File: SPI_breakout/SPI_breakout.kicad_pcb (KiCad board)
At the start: 2 copper layers, 35 x 45 mm, 10 parts, among them J1 OPC-N3 A terminal, J2 OPC-N3 B terminal, J3 External OPC 5V input, U1 WisBlock IO Connector, U2 Adafruit 4682 microSD

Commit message: Reworking routing
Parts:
- added GAS1: Screw_Terminal_01x04, MyParts:CONN_1984633_PXC, F.Cu at (2.70, -40.8)
- J1: value OPC-N3 A terminal -> OPC-N3 A
- J2: value OPC-N3 B terminal -> OPC-N3 B
- J3: value External OPC 5V input -> External OPC 5V Input
- U1: value WisBlock IO Connector -> ~
- U2: value Adafruit 4682 microSD -> ~
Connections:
- J1 pad 1: /GND -> GND
- J2 pad 1: /GND -> GND
- J3 pad 2: /GND -> GND
- U1 pad 1: (no net) -> unconnected-(U1-NC-Pad1)
- U1 pad 10: (no net) -> unconnected-(U1-SW1-Pad10)
- U1 pad 11: (no net) -> unconnected-(U1-TXD0-Pad11)
- U1 pad 12: (no net) -> unconnected-(U1-RXD0-Pad12)
- U1 pad 13: (no net) -> unconnected-(U1-RST-Pad13)
- U1 pad 14: (no net) -> unconnected-(U1-LED1-Pad14)
- U1 pad 15: (no net) -> unconnected-(U1-LED2-Pad15)
- U1 pad 16: (no net) -> unconnected-(U1-NC-Pad16)
- U1 pad 17: (no net) -> Net-(GAS1-VCC)
- U1 pad 19: (no net) -> Net-(GAS1-SDA)
- U1 pad 2: (no net) -> unconnected-(U1-NC-Pad2)
- U1 pad 20: (no net) -> Net-(GAS1-SCL)
- U1 pad 21: (no net) -> unconnected-(U1-AIN0-Pad21)
- U1 pad 22: (no net) -> unconnected-(U1-AIN1-Pad22)
- U1 pad 23: (no net) -> unconnected-(U1-NC-Pad23)
- U1 pad 24: (no net) -> unconnected-(U1-IO7-Pad24)
- U1 pad 3: /GND -> unconnected-(U1-GND-Pad3)
- U1 pad 30: (no net) -> unconnected-(U1-NC-Pad30)
- U1 pad 32: (no net) -> unconnected-(U1-IO4-Pad32)
- U1 pad 33: (no net) -> unconnected-(U1-TXD1-Pad33)
- U1 pad 34: (no net) -> unconnected-(U1-RXD1-Pad34)
- U1 pad 35: (no net) -> Net-(GAS2-SDA)
- U1 pad 36: (no net) -> Net-(GAS2-SCL)
- U1 pad 37: (no net) -> unconnected-(U1-IO5-Pad37)
- U1 pad 38: (no net) -> unconnected-(U1-IO6-Pad38)
- U1 pad 39: /GND -> unconnected-(U1-GND-Pad39)
- U1 pad 4: /GND -> Net-(GAS2-GND)
- U1 pad 40: /GND -> GND
- U1 pad 5: (no net) -> Net-(GAS2-VCC)
- U1 pad 6: (no net) -> unconnected-(U1-3v3_S-Pad6)
- U1 pad 7: (no net) -> unconnected-(U1-NC-Pad7)
- U1 pad 8: (no net) -> unconnected-(U1-NC-Pad8)
- U1 pad 9: (no net) -> unconnected-(U1-NC-Pad9)
- U1 pad MP1: /GND -> (no net)
- U1 pad MP2: /GND -> (no net)
- U1 pad MP3: /GND -> (no net)
- U1 pad MP4: /GND -> (no net)
- U2 pad 2: /GND -> GND
- U2 pad 7: (no net) -> unconnected-(U2-DAT1-Pad7)
- U2 pad 8: (no net) -> unconnected-(U2-DAT2-Pad8)
- U2 pad 9: (no net) -> unconnected-(U2-DET-Pad9)
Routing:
- net Net-(GAS1-SCL): track 0.00 -> 28.1 mm, vias 0 -> 2
- net /SPI_MISO: track 65.2 -> 40.0 mm, vias 3 -> 2
- net /SPI_MOSI: track 56.6 -> 34.6 mm, vias 3 -> 2
- net Net-(GAS1-SDA): track 0.00 -> 21.3 mm
- net Net-(GAS1-VCC): track 0.00 -> 17.9 mm, vias 0 -> 1
- net /OPC1_CS: track 43.7 -> 34.6 mm, vias 0 -> 2
- net GND: track 0.00 -> 7.01 mm
- net /OPC2_CS: track 20.0 -> 20.7 mm
- added copper zone on B.Cu, net GND
- added copper zone on F.Cu, net GND
- removed copper zone on B.Cu, net /GND
- removed copper zone on F.Cu, net /GND
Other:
- board text added: "EFD"
- board text removed: "RAK holes"

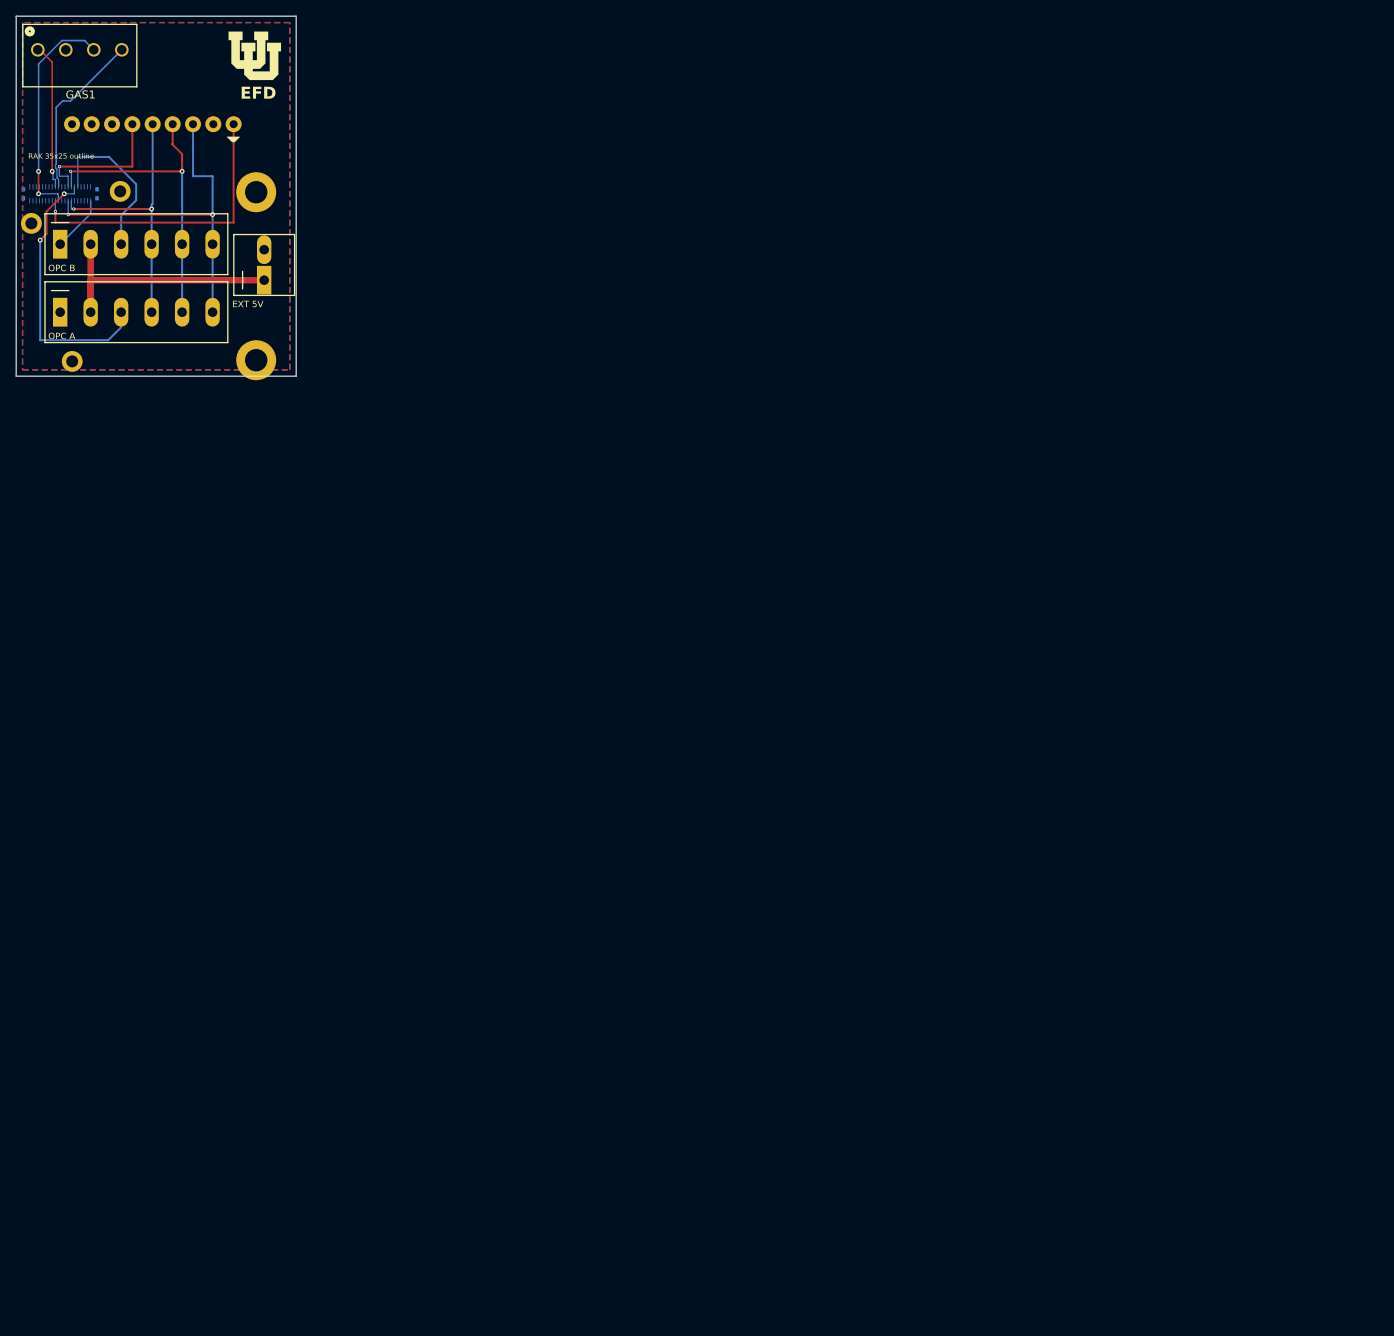
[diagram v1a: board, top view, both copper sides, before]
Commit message: Rework into smaller footprint and add 3D models
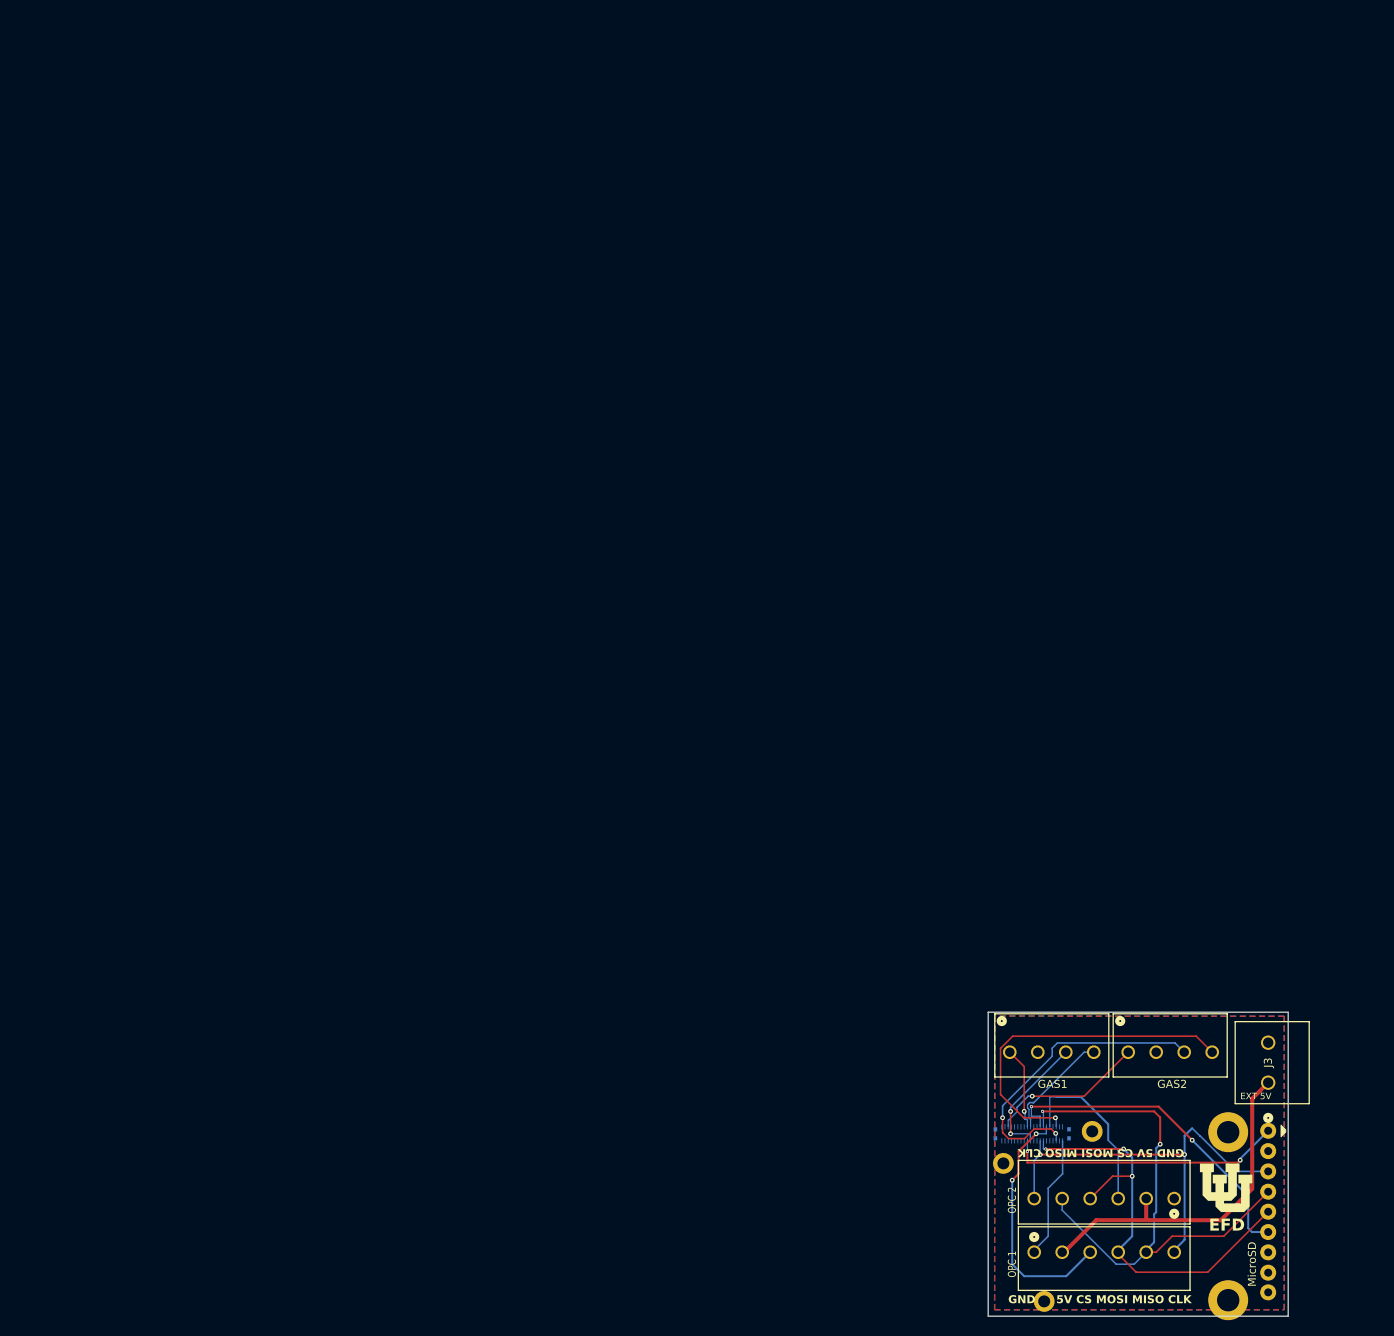
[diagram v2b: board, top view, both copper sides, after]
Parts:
- added GAS2: Screw_Terminal_01x04, MyParts:CONN_1984633_PXC, F.Cu at (139.0, 84.5)
- J1: value OPC-N3 A -> OPC 1; footprint Connector_Phoenix_MC:PhoenixContact_MC_1,5_6-G-3.81_1x06_P3.81mm_Horizontal -> MyParts:CONN_1984659_PXC
- J2: value OPC-N3 B -> OPC 2; footprint Connector_Phoenix_MC:PhoenixContact_MC_1,5_6-G-3.81_1x06_P3.81mm_Horizontal -> MyParts:CONN_1984659_PXC
- J3: footprint Connector_Phoenix_MC:PhoenixContact_MC_1,5_2-G-3.81_1x02_P3.81mm_Horizontal -> MyParts:CONN_1935161_PXC
- U2: value ~ -> MicroSD
- moved U2 194.8 mm to (156.5, 104.5), turned to -90 degrees
- moved J2 183.4 mm to (144.8, 102.8), turned to 180 degrees
- moved GAS1 174.5 mm to (124.2, 84.5)
- moved J1 169.2 mm to (127.2, 109.5)
- moved H1 169.0 mm to (128.5, 115.7)
- moved H2 169.0 mm to (151.5, 115.5)
- moved H3 169.0 mm to (134.5, 94.4)
- moved H4 169.0 mm to (123.4, 98.4)
- moved H5 169.0 mm to (151.5, 94.5)
- moved U1 169.0 mm to (127.0, 94.7)
- moved J3 160.7 mm to (156.5, 88.3)
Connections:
- U1 pad 4: Net-(GAS2-GND) -> unconnected-(U1-GND-Pad4)
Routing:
- net Net-(GAS2-SDA): track 0.00 -> 42.9 mm, vias 0 -> 1
- net Net-(GAS2-SCL): track 0.00 -> 39.0 mm, vias 0 -> 2
- net /SPI_MISO: track 40.0 -> 68.6 mm
- net /SD_CS: track 18.0 -> 42.1 mm, vias 1 -> 2
- net /SPI_MOSI: track 34.6 -> 54.8 mm, vias 2 -> 3
- net Net-(GAS2-VCC): track 0.00 -> 19.7 mm, vias 0 -> 1
- net Net-(GAS1-SCL): track 28.1 -> 16.4 mm
- net /OPC_5V_EXT: track 34.2 -> 44.2 mm
- net GND: track 7.01 -> 15.4 mm
- net /SPI_CLK: track 45.7 -> 53.9 mm
- net Net-(GAS1-VCC): track 17.9 -> 10.4 mm
- net Net-(GAS1-SDA): track 21.3 -> 14.0 mm
- net /OPC1_CS: track 34.6 -> 31.4 mm
- net Net-(U2-3v3): track 37.3 -> 34.6 mm, vias 1 -> 2
- net /OPC2_CS: track 20.7 -> 22.2 mm
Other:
- board size 35 x 45 mm -> 37.5 x 38 mm
- board text added: "5V CS MOSI MISO CLK"
- board text added: "GAS2"
- board text added: "GND"
- board text added: "GND 5V CS MOSI MISO CLK"
- board text added: "SDA1 SCL1 GND VCC"
- board text added: "SDA2 SCL1 GND VCC"
- board text removed: "OPC A"
- board text removed: "OPC B"
- board text removed: "RAK 35x25 outline"

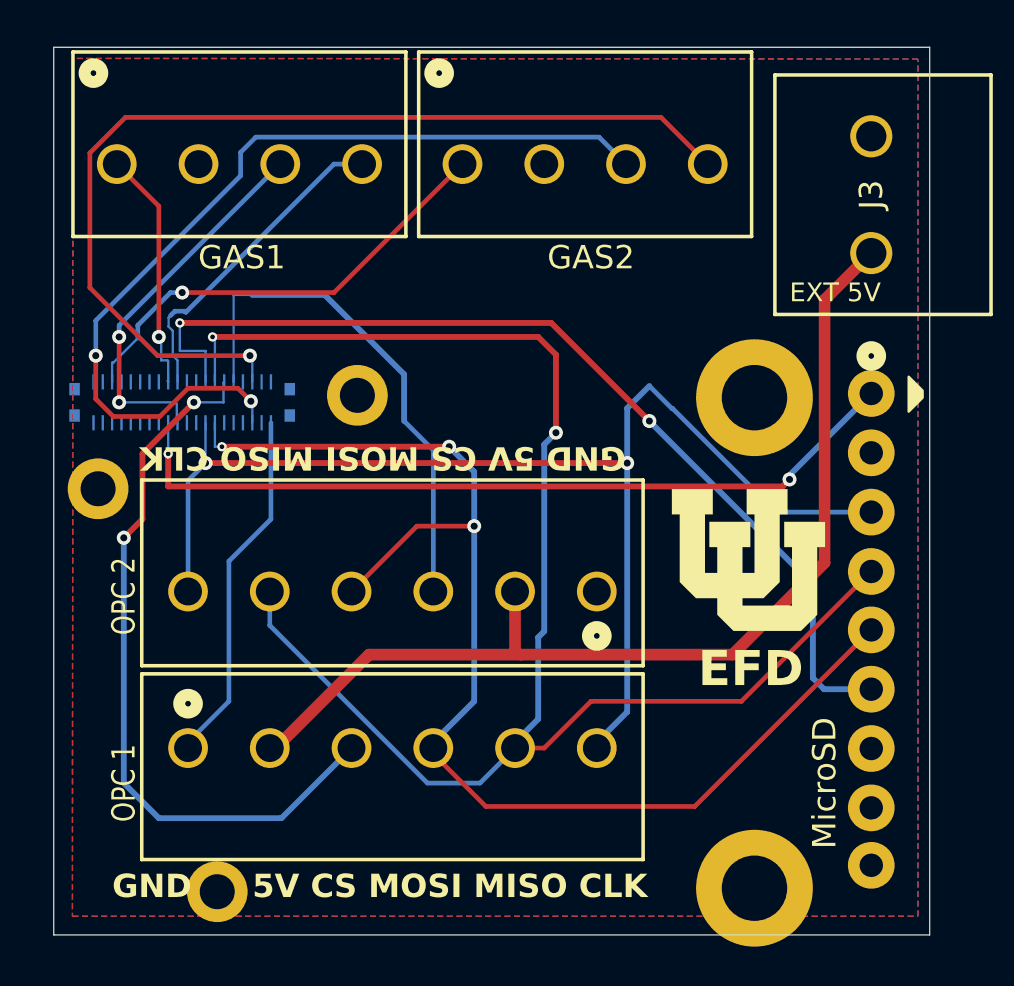
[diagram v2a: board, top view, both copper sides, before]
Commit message: Cleaning up routes
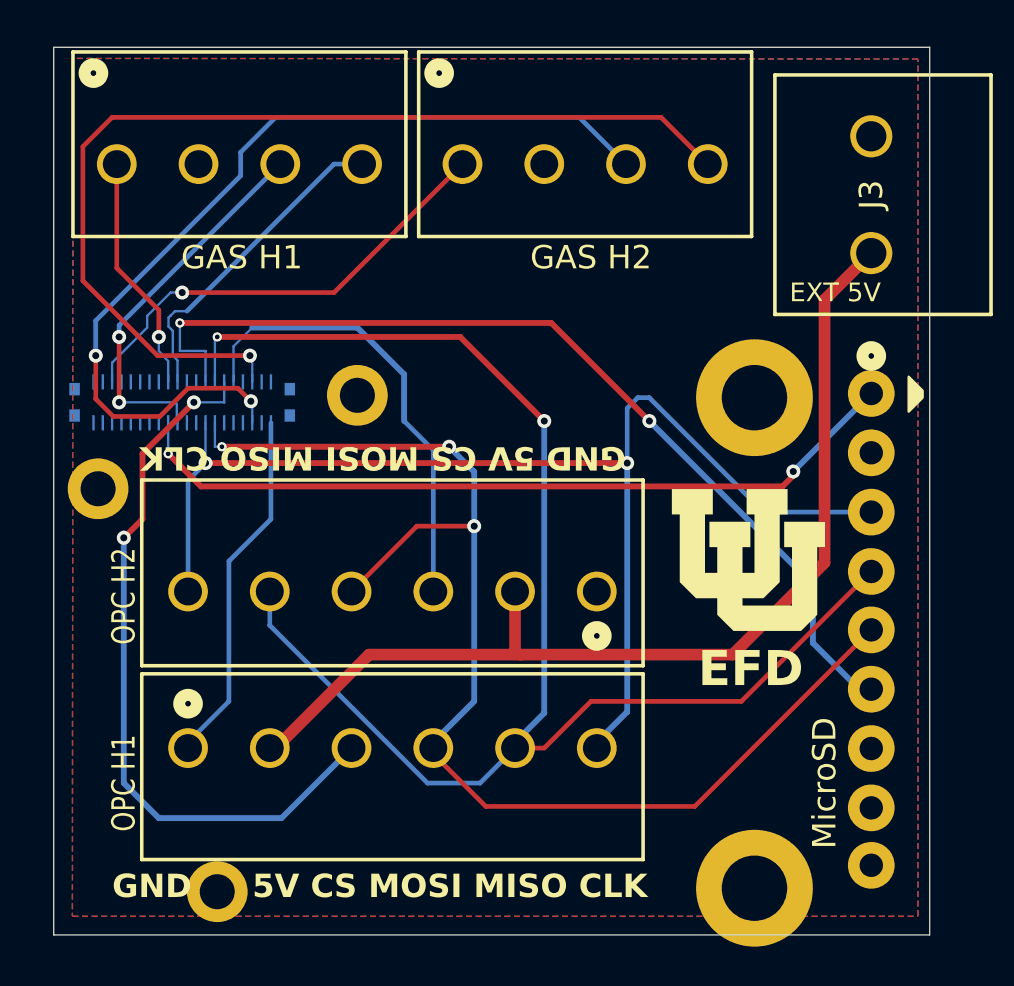
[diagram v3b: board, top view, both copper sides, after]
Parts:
- GAS H1: renamed from GAS1
- J1: value OPC 1 -> OPC H1
- J2: value OPC 2 -> OPC H2
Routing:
- net /SPI_MISO: track 68.6 -> 66.0 mm
- net /OPC2_CS: track 22.2 -> 19.8 mm
- net /SD_CS: track 42.1 -> 41.2 mm
- net Net-(U2-3v3): track 34.6 -> 33.8 mm
- net Net-(GAS2-SCL): track 39.0 -> 39.7 mm
- net Net-(GAS2-SDA): track 42.9 -> 43.5 mm
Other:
- board text added: "GAS H2"
- board text removed: "GAS2"

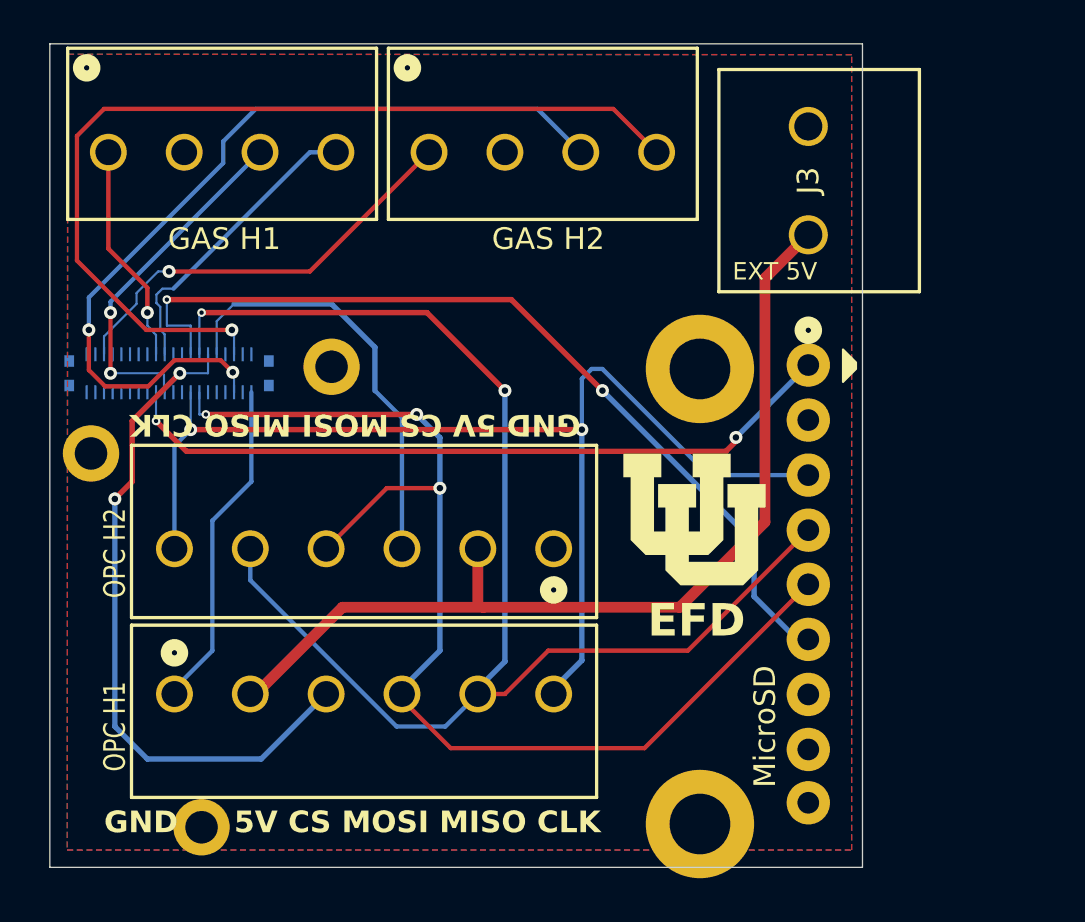
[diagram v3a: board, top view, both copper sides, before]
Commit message: Added power switching and bigger pad for SD mount
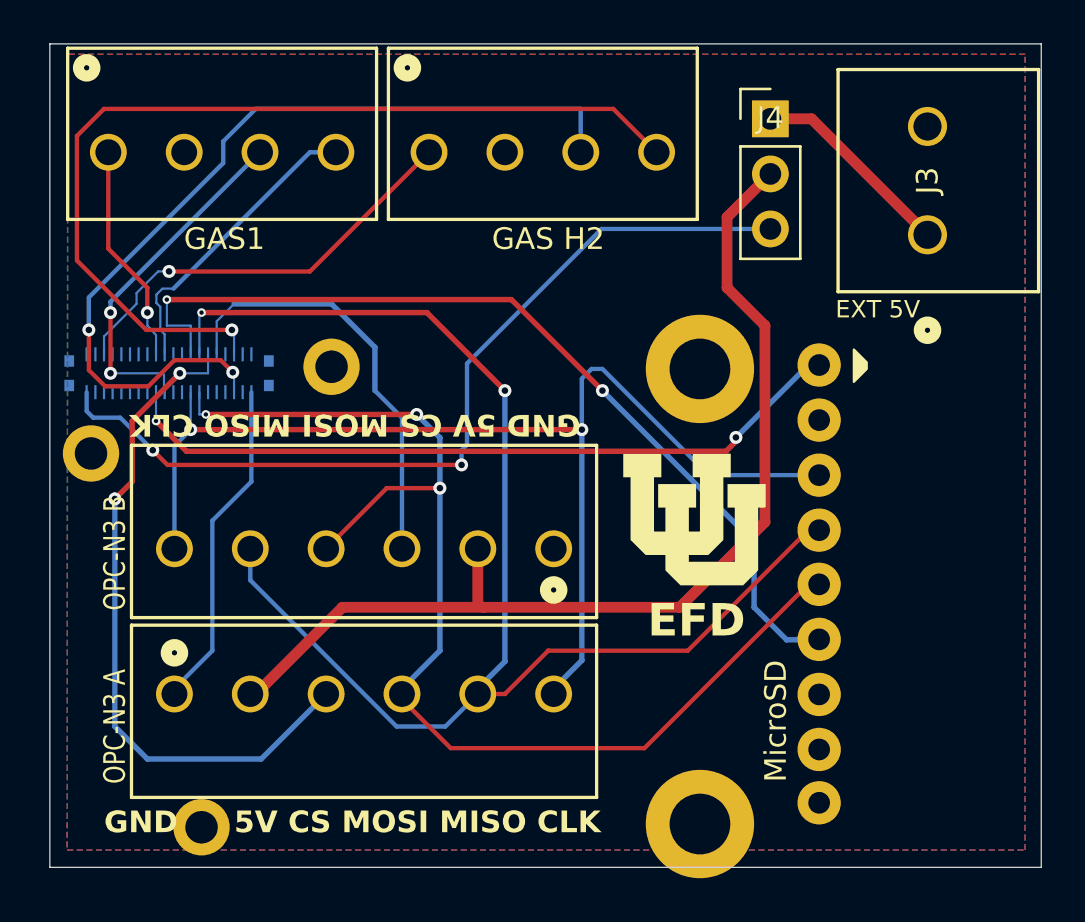
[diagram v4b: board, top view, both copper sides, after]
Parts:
- added J4: Jumper, Connector_PinHeader_2.54mm:PinHeader_1x03_P2.54mm_Vertical, F.Cu at (154.8, 83.0)
- GAS1: renamed from GAS H1
- J1: value OPC H1 -> OPC-N3 A
- J2: value OPC H2 -> OPC-N3 B
- moved J3 5.50 mm to (162.0, 88.3)
- moved U2 0.50 mm to (157.0, 104.5)
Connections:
- J1 pad 2: /OPC_5V_EXT -> /OPC_5V
- J2 pad 2: /OPC_5V_EXT -> /OPC_5V
- J3 pad 1: /OPC_5V_EXT -> /EXT_5V
- U1 pad 2: unconnected-(U1-NC-Pad2) -> Net-(J4-VBAT)
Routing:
- net /OPC_5V: track 0.00 -> 47.7 mm
- net /OPC_5V_EXT: track 44.2 -> 0.00 mm
- net Net-(J4-VBAT): track 0.00 -> 40.6 mm, vias 0 -> 2
- net /EXT_5V: track 0.00 -> 9.47 mm
- net /SD_CS: track 41.2 -> 43.0 mm
- net Net-(GAS2-SCL): track 39.7 -> 40.9 mm
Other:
- board size 37.5 x 38 mm -> 45.8 x 38 mm
